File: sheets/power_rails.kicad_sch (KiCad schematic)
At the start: 0 parts

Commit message: Buck A config
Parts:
- added C10, C11, C12: 100nF, symbol Device:C
- added C13: 18nF, symbol Device:C
- added C14: 82pF, symbol Device:C
- added C15: 8.2nF, symbol Device:C
- added R14: 33.2k, symbol Device:R
- added R15, R16: 100k, symbol Device:R
- added R17: 560k, symbol Device:R
- added R18: 10k, symbol Device:R
- added R19: 14K, symbol Device:R
- added R20: 2k, symbol Device:R
- added U6: LM5145RGYT, RGY0020B, symbol poe-aes67-amp:LM5145RGYT
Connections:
- new net: C13.1, C14.1, R19.2
- new net: C13.2, C14.2, R20.2
- new net: C10.1, C11.1, R14.1
- new net: C10.2, U6.3 (SS_TRK)
- new net: C15.1, R19.1, U6.4 (COMP)
- new net: C15.2, R20.1
- new net: C12.1, U6.17 (BST)
- new net: C11.2, U6.14 (VCC)
- new net: R15.2, R18.1
- new net: R17.2, R18.2, U6.5 (FB)
- new net: R14.2, U6.2 (RT)
- new net: R15.1, U6.11 (ILIM)
- new net BUCK_A_EN: U6.1 (EN_UVLO)
- new net BUCK_A_PG: R16.2, U6.10 (PGOOD)
- new net GND: U6.6 (AGND)
- new net GNDPWR: U6.12 (PGND), U6.15 (EP), U6.21 (EP)
- new net SW_A: C12.2
- new net V34: R17.1
- new net VCC: R16.1
- no-connect marks 0 -> 4

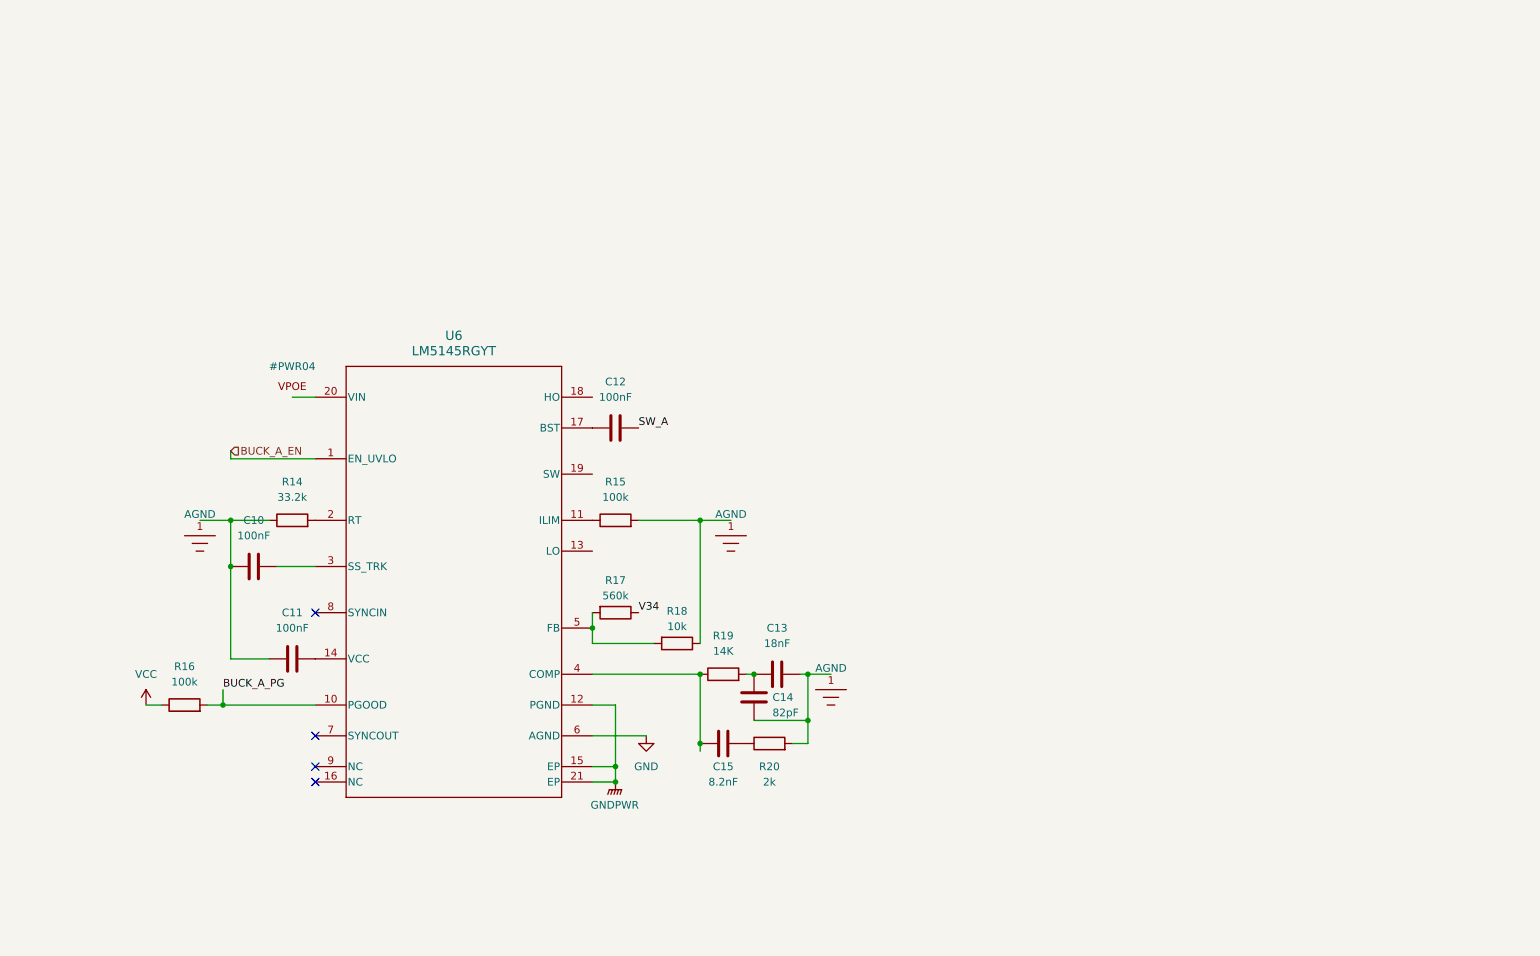
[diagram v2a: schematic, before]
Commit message: Complete Sheet 3 - Power Rails (Buck A and Buck B)
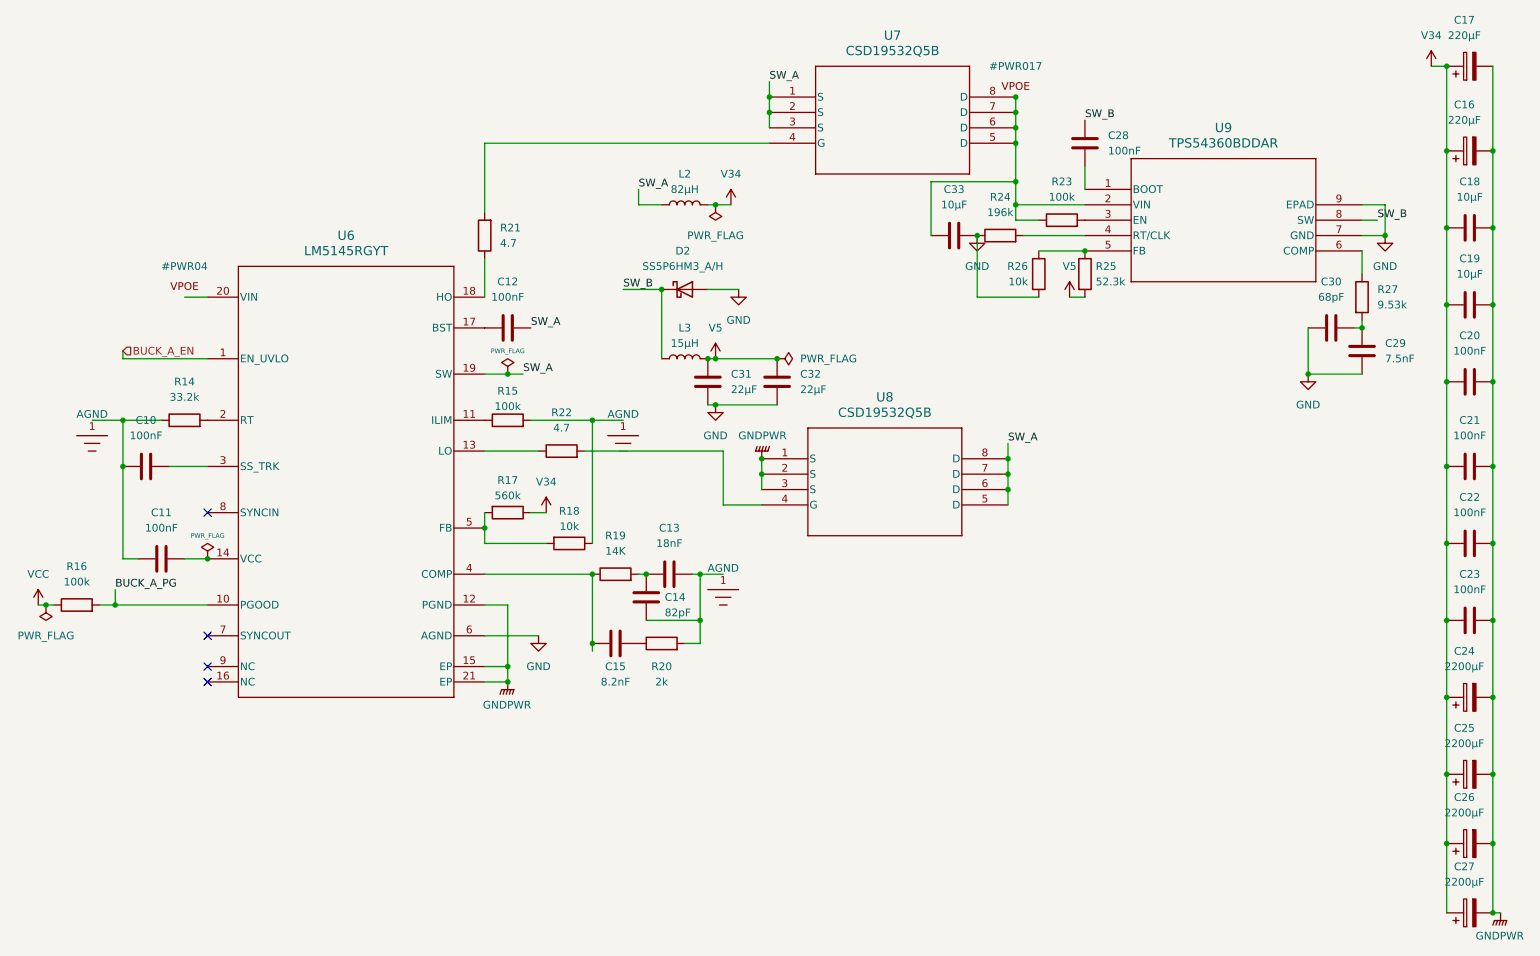
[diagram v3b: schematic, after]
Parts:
- added C16, C17: 220µF, symbol Device:C_Polarized
- added C18, C19, C33: 10µF, symbol Device:C
- added C20, C21, C22, C23, C28: 100nF, symbol Device:C
- added C24, C25, C26, C27: 2200µF, symbol Device:C_Polarized
- added C29: 7.5nF, symbol Device:C
- added C30: 68pF, symbol Device:C
- added C31, C32: 22µF, symbol Device:C
- added D2: SS5P6HM3_A/H, symbol Device:D_Schottky
- added L2: 82µH, symbol Device:L
- added L3: 15µH, symbol Device:L
- added R21, R22: 4.7, symbol Device:R
- added R23: 100k, symbol Device:R
- added R24: 196k, symbol Device:R
- added R25: 52.3k, symbol Device:R
- added R26: 10k, symbol Device:R
- added R27: 9.53k, symbol Device:R
- added U7, U8: CSD19532Q5B, DNK8, symbol poe-aes67-amp:CSD19532Q5B
- added U9: TPS54360BDDAR, U_DDA_TEX, symbol poe-aes67-amp:TPS54360BDDAR
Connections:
- net GND: now also C29.2, C30.1, C31.2, C32.2, C33.2, D2.2 (A), R24.1, R26.2, U9.7 (GND), U9.9 (EPAD)
- net GNDPWR: now also C16.2, C17.2, C18.2, C19.2, C20.2, C21.2, C22.2, C23.2, C24.2, C25.2, C26.2, C27.2, U8.1 (S), U8.2 (S), U8.3 (S)
- net SW_A: now also U6.19 (SW), L2.1, U7.1 (S), U7.2 (S), U7.3 (S), U8.5 (D), U8.6 (D), U8.7 (D), U8.8 (D)
- net V34: now also C16.1, C17.1, C18.1, C19.1, C20.1, C21.1, C22.1, C23.1, C24.1, C25.1, C26.1, C27.1, L2.2
- net at U6.13 (LO): now also R22.1
- net at U6.18 (HO): now also R21.1
- new net: R21.2, U7.4 (G)
- new net: C29.1, C30.2, R27.2
- new net: C28.2, U9.1 (BOOT)
- new net: C33.1, R23.1, U7.5 (D), U7.6 (D), U7.7 (D), U7.8 (D), U9.2 (VIN)
- new net: R23.2, U9.3 (EN)
- new net: R24.2, U9.4 (RT/CLK)
- new net: R25.1, R26.1, U9.5 (FB)
- new net: R27.1, U9.6 (COMP)
- new net: R22.2, U8.4 (G)
- new net SW_B: C28.1, D2.1 (K), L3.1, U9.8 (SW)
- new net V5: C31.1, C32.1, L3.2, R25.2
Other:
- moved on the sheet: C10, C11, C12, C13, C14, C15, R14, R15, R16, R17, R18, R19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

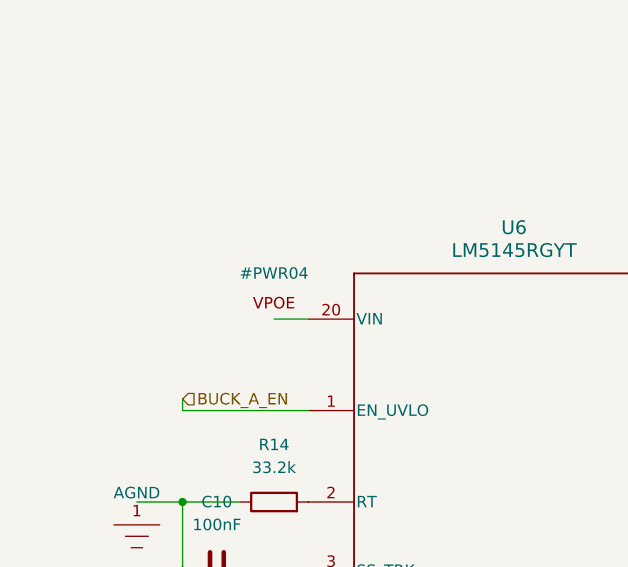
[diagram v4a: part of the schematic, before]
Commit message: Complete datasheet audit and fixes across Sheets 2, 3 and 4
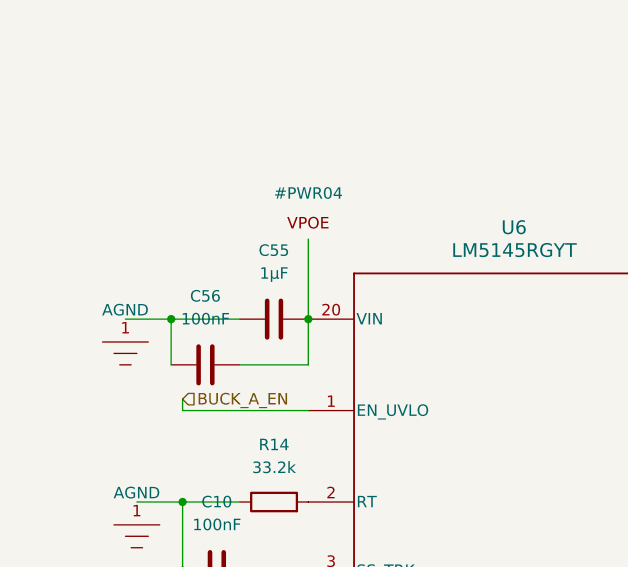
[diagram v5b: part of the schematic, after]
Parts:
- added C55: 1µF, symbol Device:C
- added C56: 100nF, symbol Device:C
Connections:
- net at U6.20 (VIN): now also C55.2, C56.2
- new net: C55.1, C56.1
